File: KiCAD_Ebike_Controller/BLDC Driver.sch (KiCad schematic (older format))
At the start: 28 parts

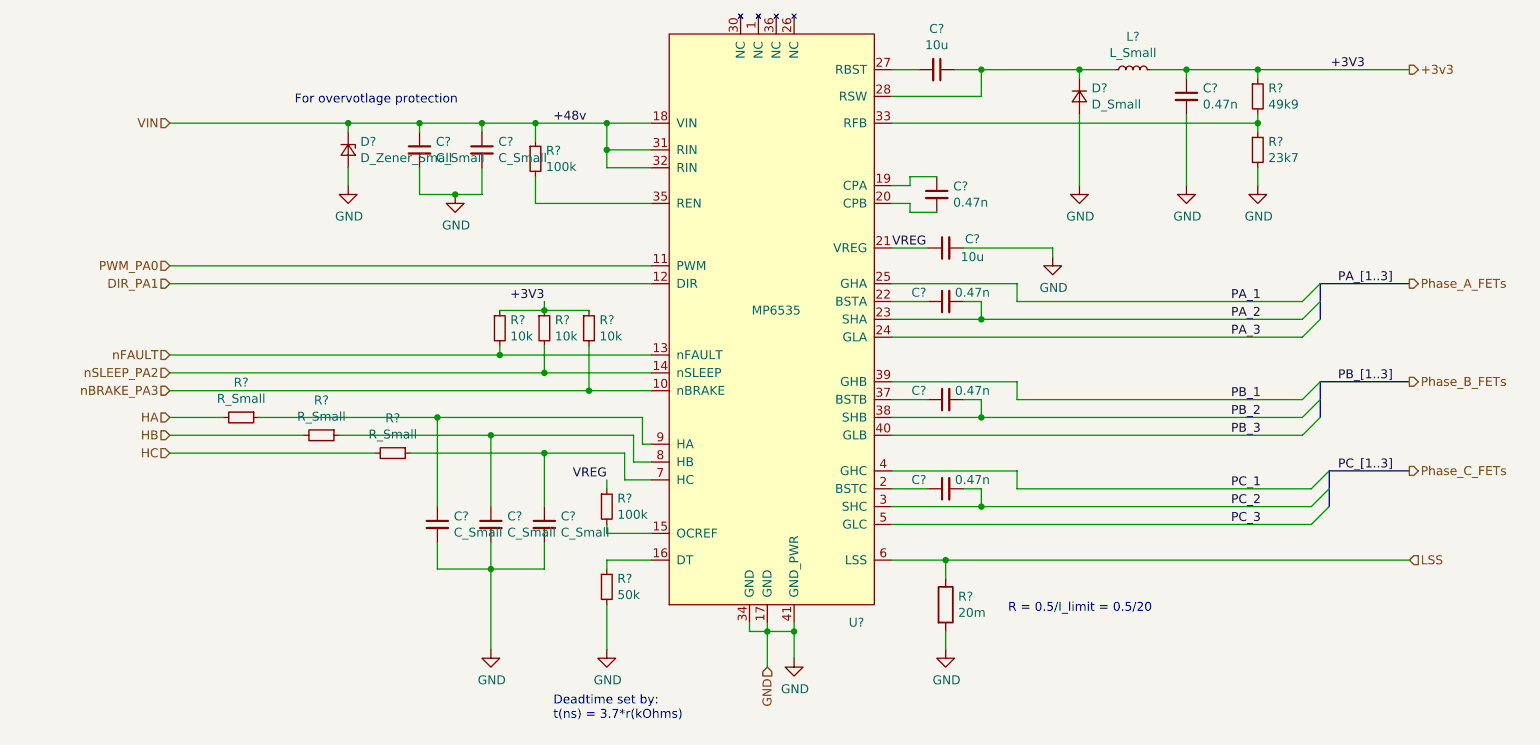
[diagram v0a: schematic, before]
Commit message: close to being done, need to add current pull ups on i2c
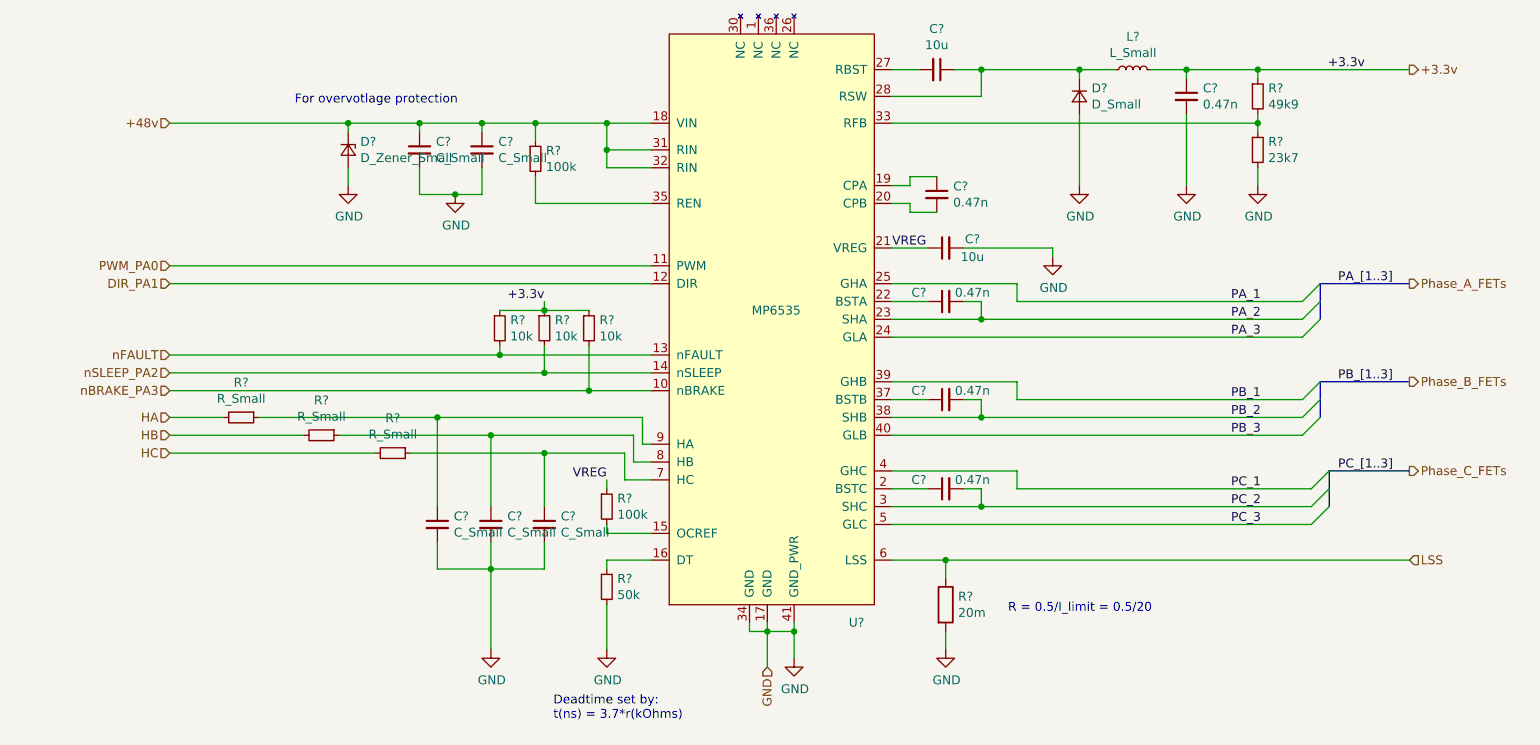
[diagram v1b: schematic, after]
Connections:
- net +3v3 renamed +3.3v
- net VIN renamed +48v
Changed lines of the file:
@@
 	4650 2700 4800 2700
 Text Label 5150 3300 2    50   ~ 0
-+3V3
++3.3v
 Wire Wire Line
 	7100 3950 7600 3950
@@
 	3050 3100 5750 3100
 Text HLabel 3050 2300 0    50   Input ~ 0
-VIN
++48v
 Text Notes 5200 5650 0    50   ~ 0
 Deadtime set by:\nt(ns) = 3.7*r(kOhms)
@@
 Wire Wire Line
 	5100 2300 5500 2300
-Text Label 5200 2300 0    50   ~ 0
-+48v
 Wire Wire Line
 	7100 4750 7400 4750
@@
 Connection ~ 9150 2000
 Text Label 9750 2000 2    50   ~ 0
-+3V3
++3.3v
 Text HLabel 10000 2000 2    50   Output ~ 0
-+3v3
++3.3v
 Text Notes 7750 5050 0    50   ~ 0
 R = 0.5/I_limit = 0.5/20

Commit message: schem done
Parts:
- removed C? (x3): C_Small, symbol Device:C_Small
- removed R? (x3): R_Small, symbol Device:R_Small
- added C?: 100n, symbol Device:C_Small
- added C? (x2): C_Small, symbol Device:C_Small
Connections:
- net GND: now also C?.2, C?.2, C?.2
- net HA: now also U?.9 (HA)
- net HB: now also U?.8 (HB)
- net HC: now also U?.7 (HC)
- net nBRAKE_PA3: now also C?.1
- net nFAULT: now also C?.1
- net nSLEEP_PA2: now also C?.1
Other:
- moved on the sheet: C?, D?

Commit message: adding footprints
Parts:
- added C?: 100u, symbol Device:C_Small
- added C?: 100n, symbol Device:C_Small
- C12, C13, C15: renamed from C?; footprint (none) -> Capacitor_SMD:C_0805_2012Metric
- C14: renamed from C?; value C_Small -> 470u; footprint (none) -> Capacitor_SMD:CP_Elec_16x17.5
- C16: renamed from C?; value C_Small -> 47u; footprint (none) -> Capacitor_SMD:CP_Elec_8x10
- C17, C18, C19, C20, C21, C22, C23: renamed from C?; footprint (none) -> Capacitor_SMD:C_0805_2012Metric_Pad1.15x1.40mm_HandSolder
- D7: renamed from D?; value D_Zener_Small -> BZX384C56
- gave numbers to parts that had none: 12
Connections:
- net +48v: now also C?.1, C?.1
- net GND: now also C?.2, C?.2
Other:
- note added: "HES are filtered in the\nMCU block"
- moved on the sheet: C14, C16, D7

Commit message: 50% of the way through the layout
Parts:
- C12: footprint Capacitor_SMD:C_0805_2012Metric -> Capacitor_SMD:C_0805_2012Metric_Pad1.15x1.40mm_HandSolder
- C13, C15: value C_Small -> 100n; footprint Capacitor_SMD:C_0805_2012Metric -> Capacitor_SMD:C_0805_2012Metric_Pad1.15x1.40mm_HandSolder
- C23: value 0.47n -> 22u
- C30: renamed from C?; footprint (none) -> Capacitor_SMD:CP_Elec_16x17.5
- C31: renamed from C?; footprint (none) -> Capacitor_SMD:C_0805_2012Metric_Pad1.15x1.40mm_HandSolder
- D7: footprint (none) -> Diode_SMD:D_SOD-323
- D8: value D_Small -> STPS2L60ZFY; footprint (none) -> Diode_SMD:D_SOD-123
- L1: value L_Small -> 100u; footprint (none) -> Inductor_SMD:L_10.4x10.4_H4.8
- R21, R22, R23, R24, R25, R26, R28, R29: footprint (none) -> Resistor_SMD:R_0805_2012Metric_Pad1.15x1.40mm_HandSolder
- R27: footprint (none) -> Resistor_SMD:20m_4W
- U2: footprint (none) -> Package_DFN_QFN:QFN-40-1EP_5x5mm_P0.4mm_EP3.6x3.6mm
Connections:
- net GND: no longer C12.2, C13.2, C15.2, R26.2, U2.17 (GND), U2.34 (GND)
- net PA_1 renamed PA1
- net PA_2 renamed PA2
- net PA_3 renamed PA3
- net PB_1 renamed PB1
- net PB_2 renamed PB2
- net PB_3 renamed PB3
- net PC_1 renamed PC1
- net PC_2 renamed PC2
- net PC_3 renamed PC3
- new net GNDD: C12.2, C13.2, C15.2, R26.2, U2.17 (GND), U2.34 (GND)

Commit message: Layout done. will tidy up ref des next
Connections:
- net GND: now also U2.34 (GND)
- net GNDD: no longer U2.34 (GND)
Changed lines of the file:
@@
 $Descr A4 11693 8268
 encoding utf-8
-Sheet 7 7
+Sheet 6 7
 Title ""
 Date ""
@@
 	7600 4350 7600 4450
 Wire Wire Line
-	6300 5100 6300 5150
-Wire Wire Line
-	6300 5150 6400 5150
-Wire Wire Line
 	7400 5150 7400 5250
 Wire Wire Line
@@
 Wire Wire Line
 	7400 4750 7400 4850
-Wire Wire Line
-	6400 5100 6400 5150
 Wire Wire Line
 	7350 2800 7200 2800
@@
 L power:GNDD #PWR0136
 U 1 1 5FE9CEF7
-P 6300 5300
-F 0 "#PWR0136" H 6300 5050 50  0001 C CNN
-F 1 "GNDD" H 6304 5145 50  0000 C CNN
-F 2 "" H 6300 5300 50  0001 C CNN
-F 3 "" H 6300 5300 50  0001 C CNN
-	1    6300 5300
-	1    0    0    -1
-$EndComp
-Wire Wire Line
-	6550 5100 6550 5300
-Wire Wire Line
-	6300 5150 6300 5300
-Connection ~ 6300 5150
+P 6400 5500
+F 0 "#PWR0136" H 6400 5250 50  0001 C CNN
+F 1 "GNDD" H 6404 5345 50  0000 C CNN
+F 2 "" H 6400 5500 50  0001 C CNN
+F 3 "" H 6400 5500 50  0001 C CNN
+	1    6400 5500
+	1    0    0    -1
+$EndComp
+Wire Wire Line
+	6550 5100 6550 5200
+Wire Wire Line
+	6400 5100 6400 5500
+Wire Wire Line
+	6550 5200 6300 5200
+Wire Wire Line
+	6300 5200 6300 5100
+Connection ~ 6550 5200
+Wire Wire Line
+	6550 5200 6550 5300
 Wire Bus Line
 	9500 3200 9500 3400

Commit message: done and gerbes sent to JLC
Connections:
- net nSLEEP_PA2 renamed nSLEEP_PA12
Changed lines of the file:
@@
 nBRAKE_PA3
 Text HLabel 2800 3700 0    50   Input ~ 0
-nSLEEP_PA2
+nSLEEP_PA12
 Text HLabel 2800 4000 0    50   Input ~ 0
 HA
